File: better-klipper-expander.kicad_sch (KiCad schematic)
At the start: 89 parts, among them J1 24V IN, J10 TH1, J11 VFAN_SEL, J2 USB4105-GF-A, J3 FAN0, J4 FAN1, J5 FAN2, J6 TH0, J7 FAN3, J8 FAN4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

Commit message: Finished V1
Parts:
- removed C15: 22uF, Capacitor_SMD:C_0805_2012Metric, symbol Device:C_Small
- removed U5: LM2940G-12V, Package_TO_SOT_SMD:SOT-223, symbol Regulator_Linear:L7812
- added D12: S1A, Diode_SMD:D_SMA, symbol Diode:1N4007
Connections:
- net +5V: now also D12.2 (A)
- net D+: no longer J2.A7 (DN1), J2.B7 (DN2), R4.1, R4.2, U4.46 (USB_DM)
- net TH0: now also U4.39 (GPIO27_ADC1); no longer U4.38 (GPIO26_ADC0)
- net TH1: now also U4.38 (GPIO26_ADC0); no longer U4.39 (GPIO27_ADC1)
- net VCC: now also D12.1 (K)
- new net D-: J2.A7 (DN1), J2.B7 (DN2), R4.1, R4.2, U4.46 (USB_DM)

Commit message: Vias, Widths, and Organization...
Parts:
- removed D12: S1A, Diode_SMD:D_SMA, symbol Diode:1N4007
- added F3: 4A, Fuse:Fuse_0805_2012Metric, symbol Device:Fuse_Small
- F1: symbol Device:Fuse -> Device:Fuse_Small
- J11: footprint (none) -> Connector_PinHeader_2.54mm:PinHeader_2x02_P2.54mm_Vertical
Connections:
- net +5V: now also F1.2, F3.2; no longer F1.1, J11.4 (Pin_4)
- net GND: now also D10.2 (A), J9.2 (Pin_2); no longer Q6.2 (S)
- net VFAN: now also Q6.2 (S); no longer D10.1 (K), J9.2 (Pin_2)
- net at C9.1, L2.1: now also F1.1; no longer F1.2
- net at J9.1 (Pin_1), Q6.3 (D): now also D10.1 (K); no longer D10.2 (A)
- new net: F3.1, J11.4 (Pin_4)
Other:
- moved on the sheet: C22, C23, C6, C9, D10, D11, D2, D4, D7, F1, F2, J1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

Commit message: Neopixelssssss....
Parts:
- removed R1: 5.1K, Resistor_SMD:R_0805_2012Metric, symbol Device:R_Small
- added J12: Neopixel, Connector_PinHeader_2.54mm:PinHeader_1x03_P2.54mm_Vertical, symbol Connector:Conn_01x03_Male
- added U5: TXS0101DBVR, SOT95P280X145-6N, symbol TXS0101DBVR:TXS0101DBVR
- F3: MANUFACTURER (none) -> TECHFUSE
- R3, R4: value 27R -> 22R
- U1: value W25Q80DVSNIG_TR -> W25Q80DVSNIG; MANUFACTURER (none) -> Winbond Elec
- U2: footprint Package_TO_SOT_SMD:SOT-23_Handsoldering -> Package_TO_SOT_SMD:SOT-23; MANUFACTURER (none) -> NATLINEAR
- U4: MANUFACTURER (none) -> Raspberry Pi Foundation
- Y1: footprint Oscillator:Oscillator_SMD_SeikoEpson_SG8002CE-4Pin_3.2x2.5mm_HandSoldering -> Oscillator:Oscillator_SMD_SeikoEpson_SG8002CE-4Pin_3.2x2.5mm; MANUFACTURER (none) -> HD
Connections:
- net +3.3V: now also U5.1 (VCCA), U5.5 (OE)
- net +5V: now also J12.1 (Pin_1), U5.6 (VCCB)
- net GND: now also J12.3 (Pin_3), U5.2 (GND)
- net VCC: now also J11.4 (Pin_4); no longer J11.3 (Pin_3)
- net XIN: now reaches C7.1, U4.20 (XIN), Y1.1
- net XOUT: now reaches U4.21 (XOUT), Y1.3
- net at F3.1: now also J11.3 (Pin_3); no longer J11.4 (Pin_4)
- net at J2.A5 (CC1): no longer J2.B5 (CC2)
- net GPIO24: now reaches U4.36 (GPIO24)
- net GPIO24: now also U5.3 (A)
- new net NEO_DATA: J12.2 (Pin_2), U5.4 (B)
- no-connect marks 29 -> 30
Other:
- moved on the sheet: C10, C11, C12, C14, C16, C18, C20, C21, C22, C23, C4, D10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

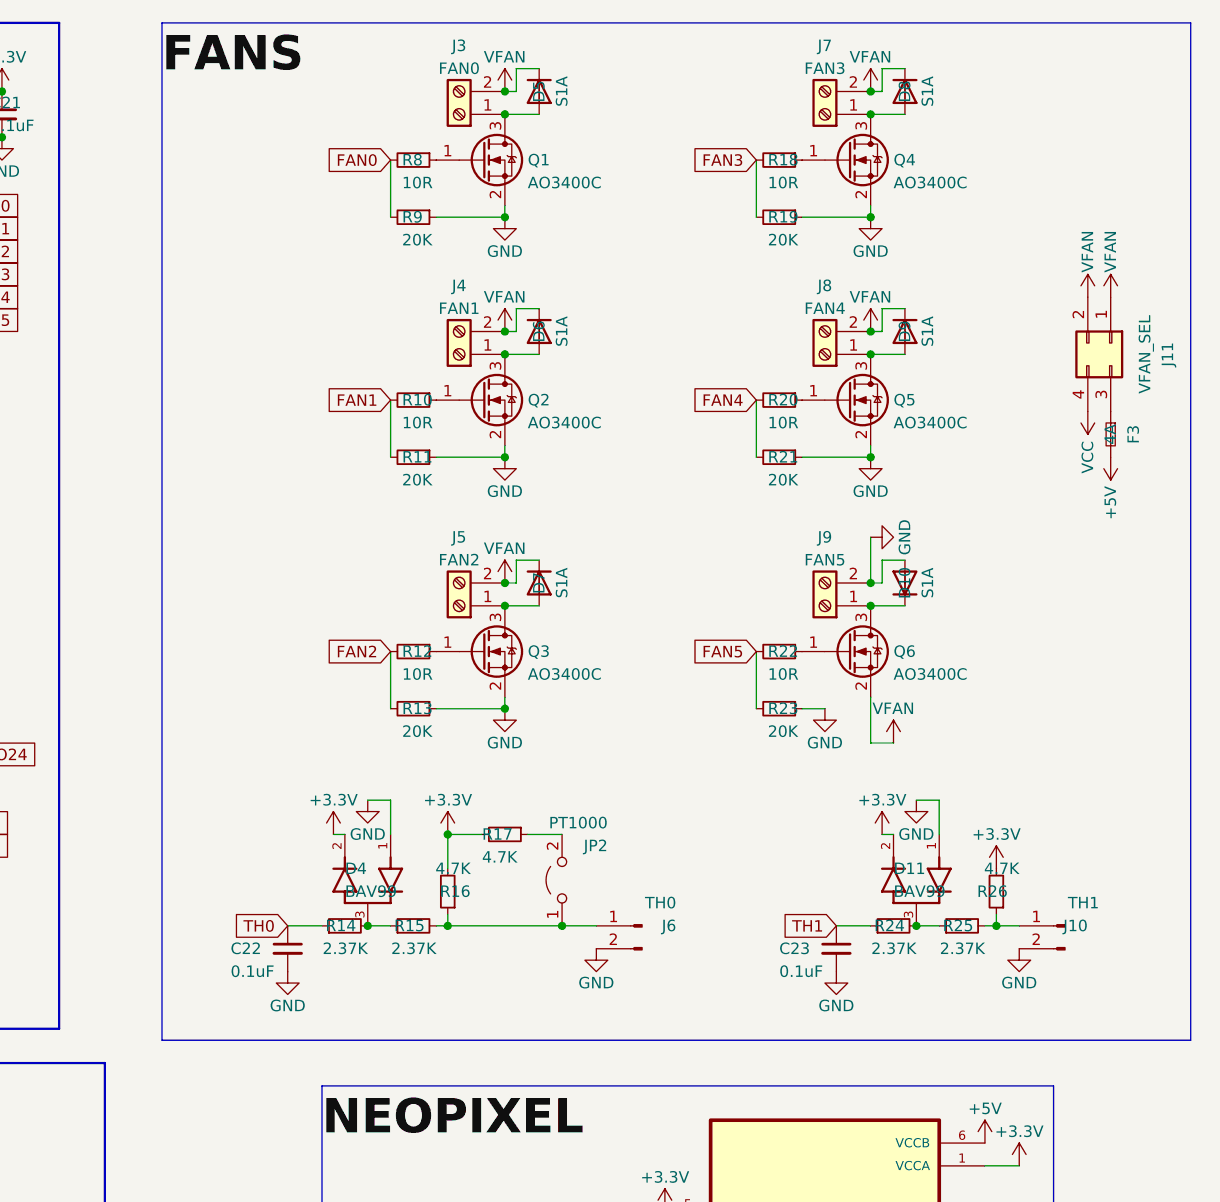
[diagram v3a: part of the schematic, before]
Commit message: 3 fans per voltage selection now
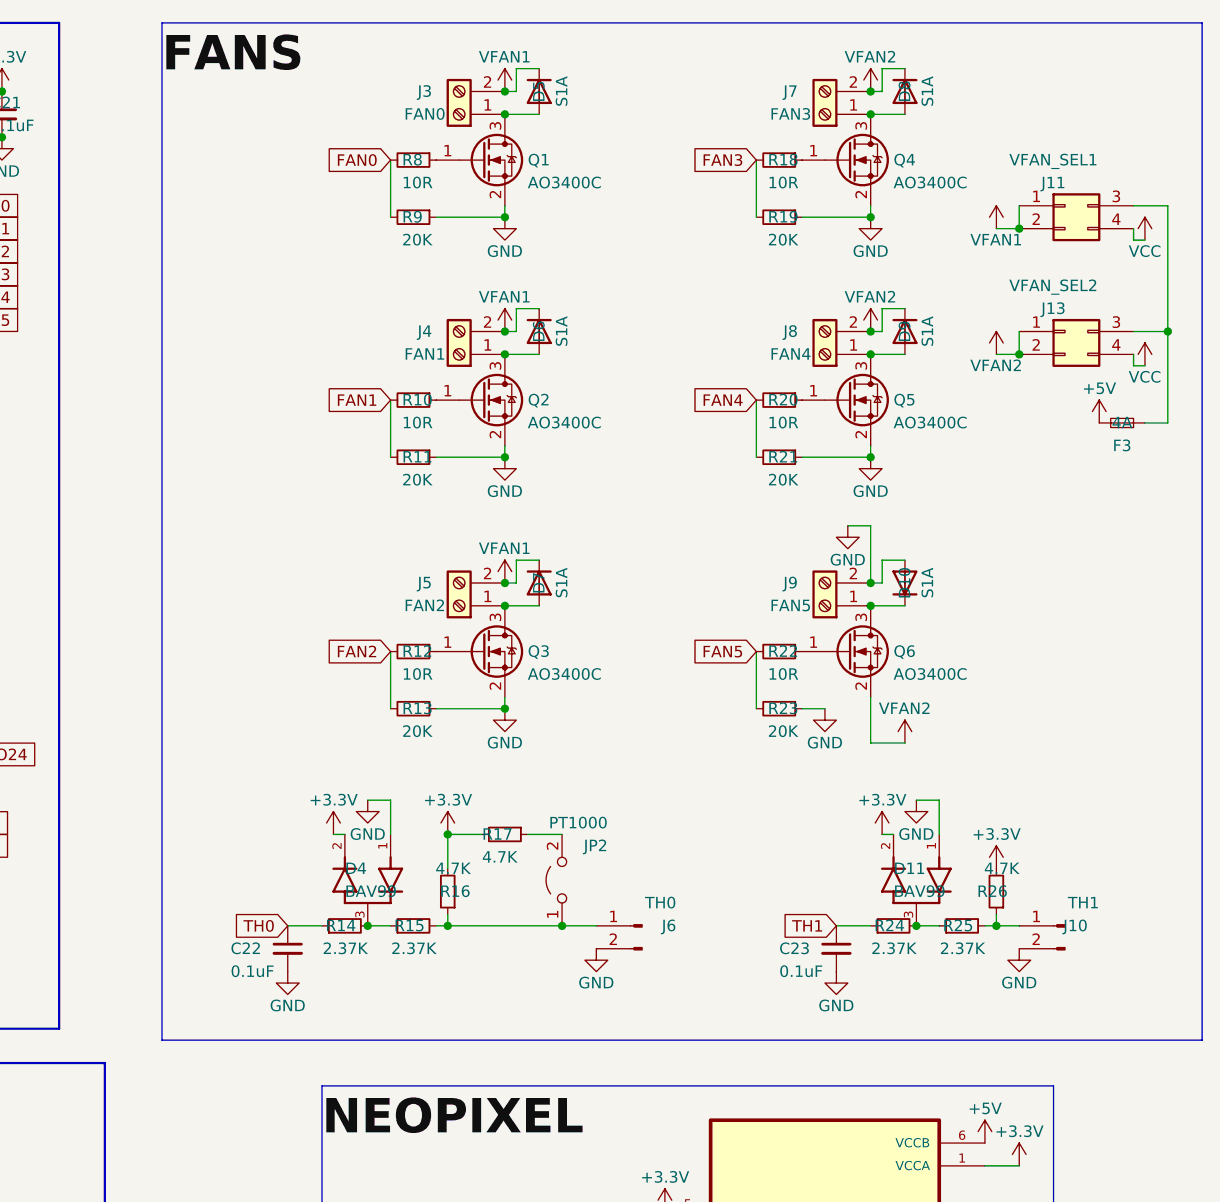
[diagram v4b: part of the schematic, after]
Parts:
- added J13: VFAN_SEL2, Connector_PinHeader_2.54mm:PinHeader_2x02_P2.54mm_Vertical, symbol Connector_Generic:Conn_02x02_Top_Bottom
- J11: value VFAN_SEL -> VFAN_SEL1
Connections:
- net VCC: now also J13.4 (Pin_4)
- net VFAN: now also J13.1 (Pin_1), J13.2 (Pin_2)
- net at F3.1, J11.3 (Pin_3): now also J13.3 (Pin_3)
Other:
- moved on the sheet: J11

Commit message: Minor updates
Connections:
- net +3.3V: now also C10.1, C11.1, C12.1, U4.23 (DVDD), U4.45 (VREG_VOUT), U4.50 (DVDD)
- net NEO_DATA: no longer names the net of J12.2 (Pin_2), U5.4 (B)
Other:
- moved on the sheet: C1, C10, C11, C12, C13, C14, C16, C17, C18, C19, C2, C20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

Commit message: change flash + fix major problem + minor cleanup
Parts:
- added C15: 0.1uF, Capacitor_SMD:C_0805_2012Metric, symbol Device:C_Small
- C7, C8: footprint Capacitor_SMD:C_0805_2012Metric -> Capacitor_SMD:C_0603_1608Metric
- U1: value W25Q80DVSNIG -> W25Q16JVUXIQ; footprint SOIC127P600X175-8N -> W25Q16JVUXIQ:SON50P300X200X60-9N
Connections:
- net GPIO24 is gone; now on net NEOPIXEL: U4.36 (GPIO24), U5.3 (A)
- net +3.3V: now also C15.2
- net VCC: no longer U1.8 (VCC)
- net VFAN: now also D10.1 (K), J9.1 (Pin_1), Q6.3 (D)
- new net: C15.1, U1.8 (VCC)
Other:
- moved on the sheet: C10, C11, C12, C14, C16, C18, C20, C21, C22, C23, C4, D10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
